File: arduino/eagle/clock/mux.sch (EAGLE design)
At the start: 64 parts, among them U1 SN74HC595N, U2 SN74HC595N, U3 SN74HC595N, U4 SN74HC595N

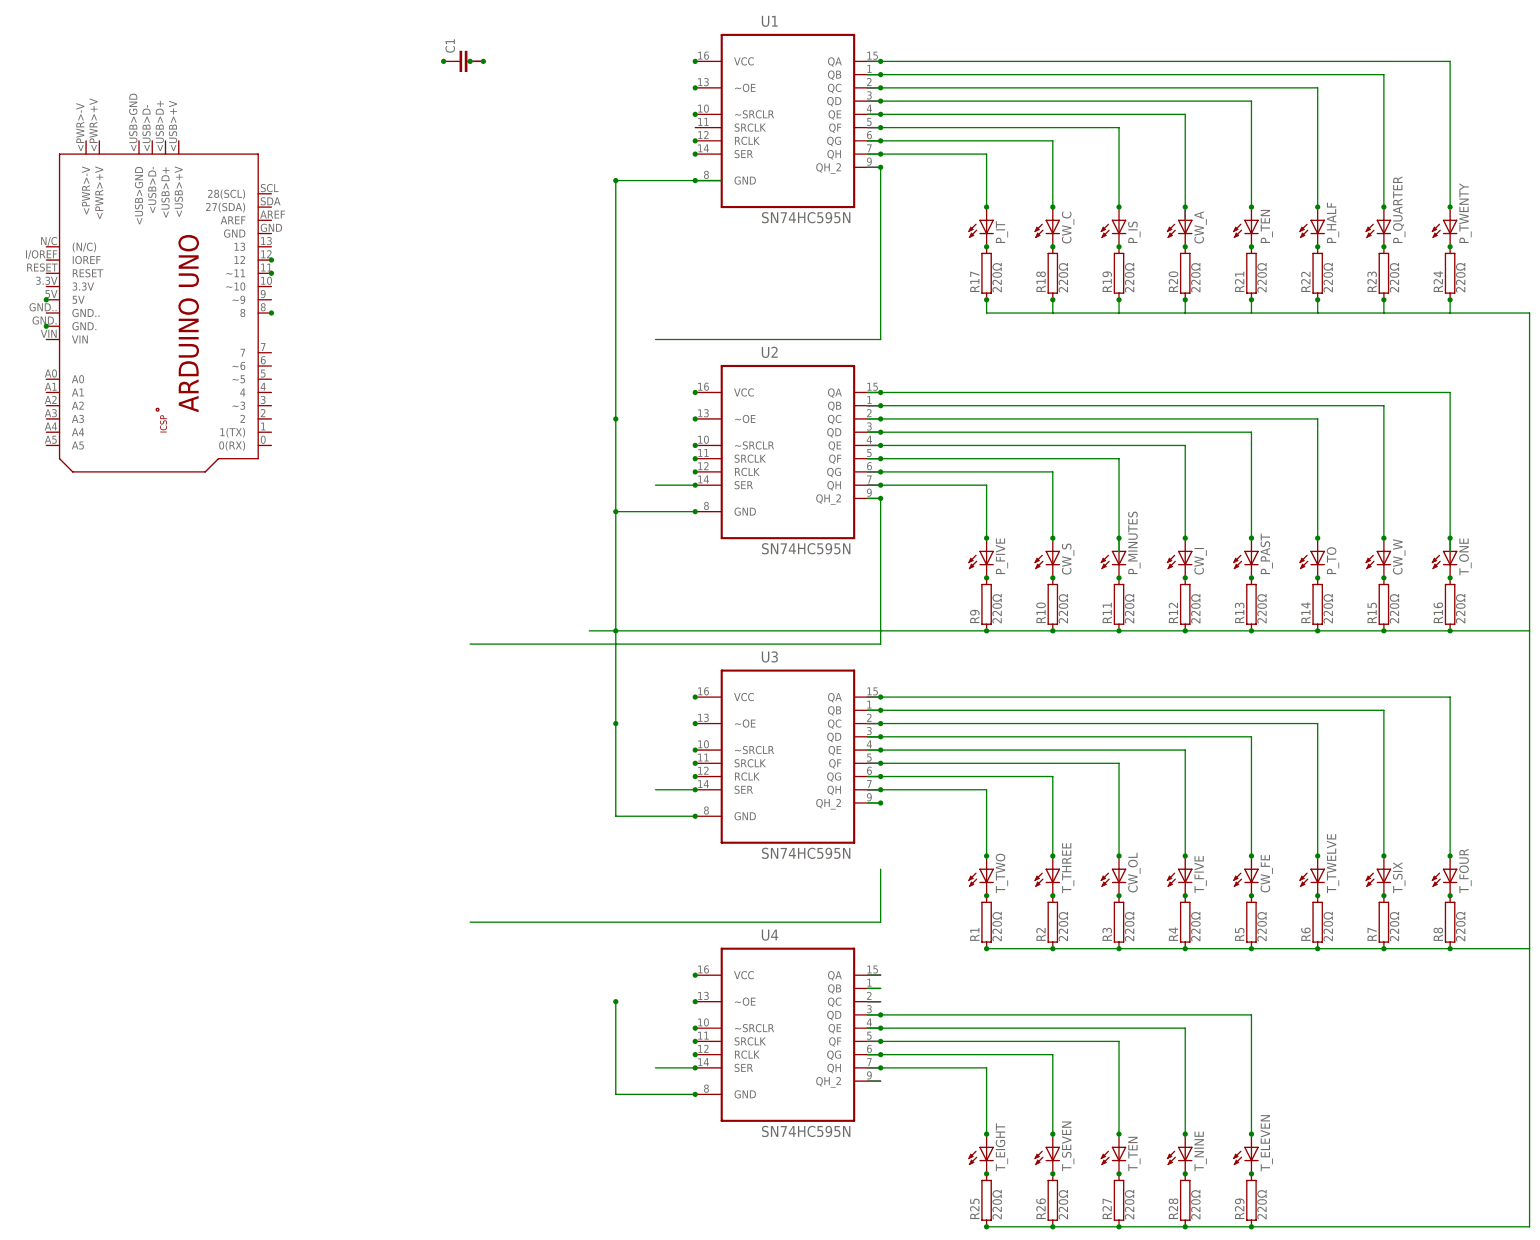
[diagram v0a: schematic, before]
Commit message: Remove LEDs from clock mux
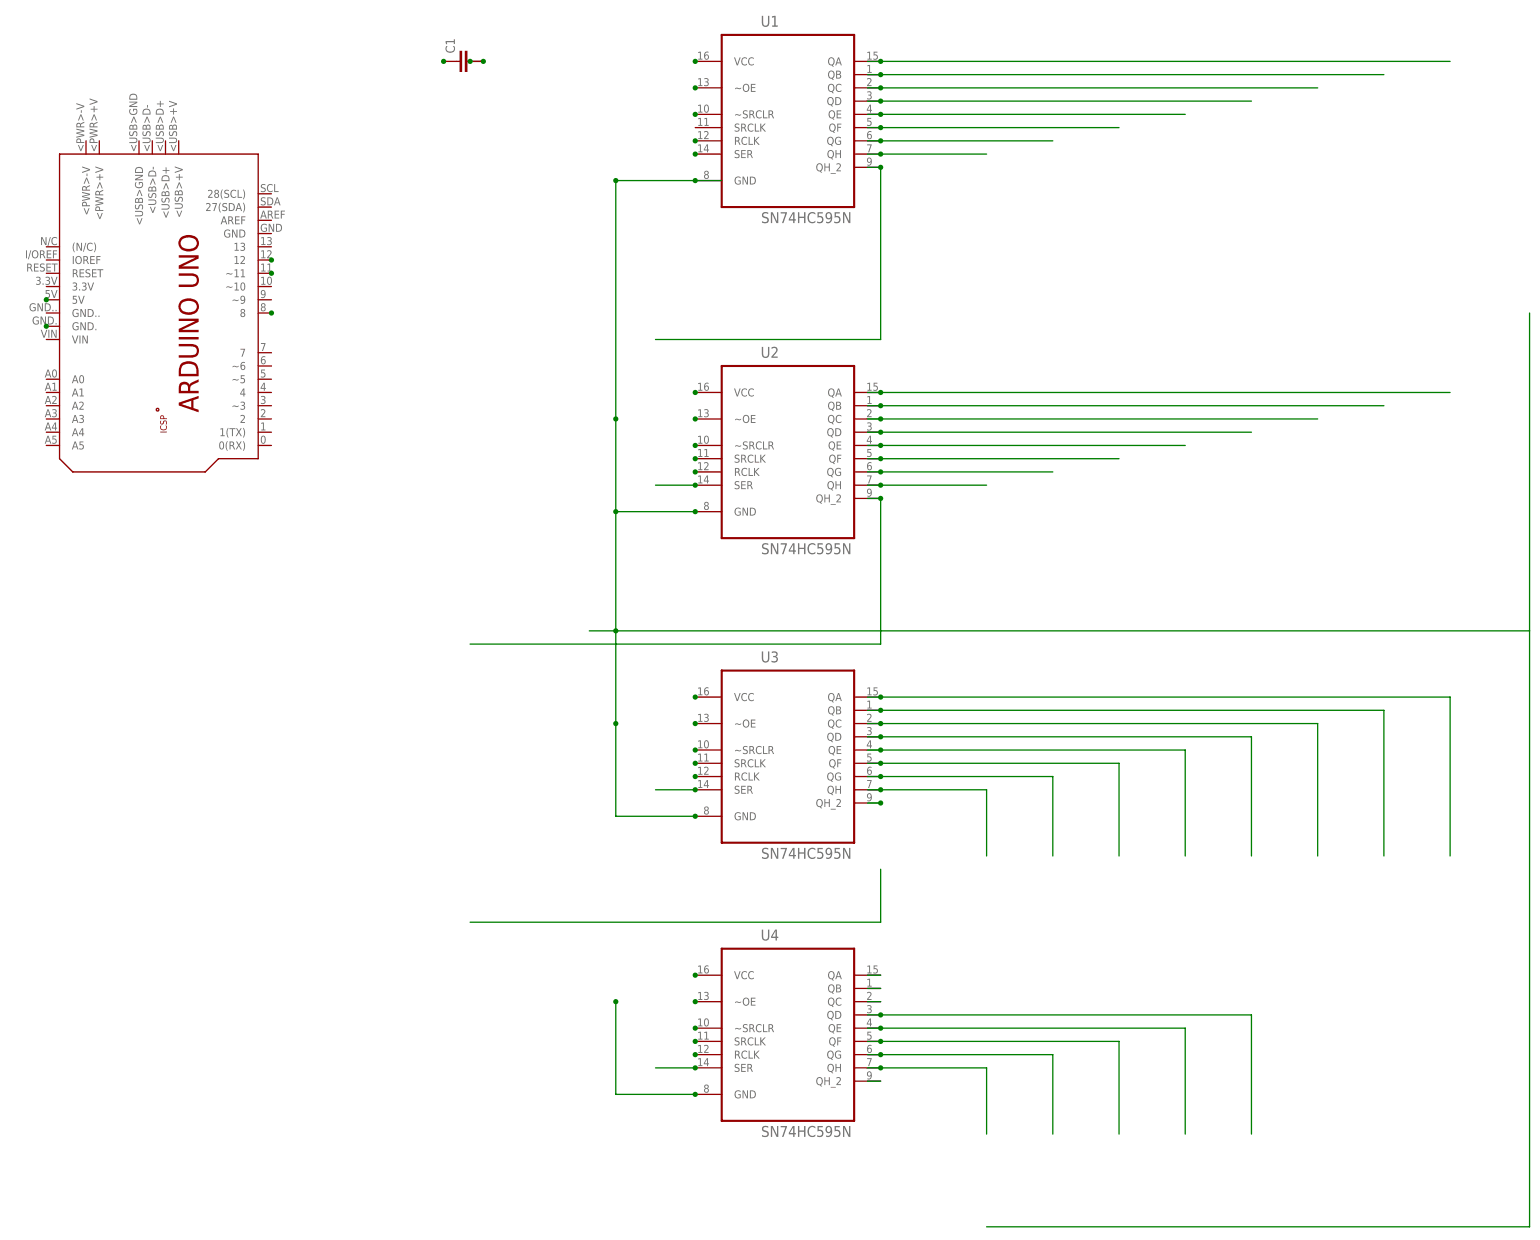
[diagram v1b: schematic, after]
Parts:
- removed CW_A, CW_C, CW_FE, CW_I, CW_OL, CW_S, CW_W, P_FIVE, P_HALF, P_IS, P_IT, P_MINUTES, P_PAST, P_QUARTER, P_TEN, P_TO, P_TWENTY, T_EIGHT, T_ELEVEN, T_FIVE, T_FOUR, T_NINE, T_ONE, T_SEVEN, T_SIX, T_TEN, T_THREE, T_TWELVE, T_TWO: (no value), led:LEDSMT1206
- removed R1, R10, R11, R12, R13, R14, R15, R16, R17, R18, R19, R2, R20, R21, R22, R23, R24, R25, R26, R27, R28, R29, R3, R4, R5, R6, R7, R8, R9: 220Ω, resistor-power:RCA4050
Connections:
- removed net CW_C: CW_C.C, R18.2
- removed net N$1: R1.2, T_TWO.C
- removed net N$10: CW_S.C, R10.2
- removed net N$11: P_MINUTES.C, R11.2
- removed net N$12: CW_I.C, R12.2
- removed net N$13: P_PAST.C, R13.2
- removed net N$14: P_TO.C, R14.2
- removed net N$15: CW_W.C, R15.2
- removed net N$16: R16.2, T_ONE.C
- removed net N$17: P_IT.C, R17.2
- removed net N$18: R25.2, T_EIGHT.C
- removed net N$19: P_IS.C, R19.2
- removed net N$2: R2.2, T_THREE.C
- removed net N$20: CW_A.C, R20.2
- removed net N$21: P_TEN.C, R21.2
- removed net N$23: P_QUARTER.C, R23.2
- removed net N$24: P_TWENTY.C, R24.2
- removed net N$3: CW_OL.C, R3.2
- removed net N$4: R4.2, T_FIVE.C
- removed net N$5: CW_FE.C, R5.2
- removed net N$7: R7.2, T_SIX.C
- removed net N$73: R26.2, T_SEVEN.C
- removed net N$74: R27.2, T_TEN.C
- removed net N$75: R28.2, T_NINE.C
- removed net N$76: R29.2, T_ELEVEN.C
- removed net N$8: R8.2, T_FOUR.C
- removed net N$9: P_FIVE.C, R9.2
- removed net T_TWELVE: R6.2, T_TWELVE.C
- net CW_W: no longer CW_W.A
- net N$22: now also U4.GND; no longer P_HALF.C, R22.2
- net N$27: no longer CW_I.A
- net N$29: no longer P_TO.A
- net N$31: no longer T_ONE.A
- net N$32: no longer P_PAST.A
- net N$33: no longer CW_S.A
- net N$34: no longer P_FIVE.A
- net N$35: no longer T_FIVE.A
- net N$36: no longer P_MINUTES.A
- net N$37: no longer T_THREE.A
- net N$38: no longer CW_OL.A
- net N$39: no longer CW_FE.A
- net N$40: no longer T_TWELVE.A
- net N$41: no longer T_SIX.A
- net N$42: no longer T_FOUR.A
- net N$43: no longer T_TWO.A
- net N$44: no longer P_TWENTY.A
- net N$52: no longer P_IT.A
- net N$53: no longer CW_C.A
- net N$54: no longer P_IS.A
- net N$55: no longer CW_A.A
- net N$56: no longer P_TEN.A
- net N$57: no longer P_QUARTER.A
- net N$58: no longer P_HALF.A
- net N$80: no longer R1.1, R10.1, R11.1, R12.1, R13.1, R14.1, R15.1, R16.1, R17.1, R18.1, R19.1, R2.1, R20.1, R21.1, R22.1, R23.1, R24.1, R25.1, R26.1, R27.1, R28.1, R29.1, R3.1, R4.1, R5.1, R6.1, R7.1, R8.1, R9.1, U4.GND
- net N$81: no longer T_SEVEN.A
- net N$82: no longer T_TEN.A
- net N$83: no longer T_ELEVEN.A
- net N$87: no longer T_NINE.A
- net N$88: no longer T_EIGHT.A
